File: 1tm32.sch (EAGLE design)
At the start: 38 parts, among them IC1 STM32L412RBT6P, IC2 BGM240PA32VNN3, J1 FTSH-107-01-L-DV-K-A, J2 10118192-0001LF, SW1 LL3301FF065QJ, U2 LD39050PU33R, Y1 8MHz, Y2 32.7KHz

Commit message: layout completed
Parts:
- removed J1: FTSH-107-01-L-DV-K-A, ce-capstone:FTSH-107-01-L-DV-K-A
- removed JP1: (no value), pinhead:PINHD-1X14
- removed R11: 220, ce-capstone:RT0402FRE07220RL
- removed R14: 10k, ce-capstone:RC0402FR-0710KL
- removed R5: 1K, ce-capstone:RC0402FR-071KL
- added J3: FTSH-105-01-L-D, FTSH-105-01-L-D(bt_connect):FTSH-105-01-L-D
- added J4: 20021321-00020C4LF, 20021321-00020C4LF(20head):20021321-00020C4LF
- added JP2: (no value), pinhead:PINHD-2X5
- added JP3: (no value), pinhead:PINHD-2X4
- added JP4: (no value), pinhead:PINHD-2X3
- added R10: 10K, RC0805JR-0710KL:RC0805JR-0710KL
- added R4: 220, RC0805FR-10220RL:RC0805FR-10220RL
- added R6, R7, R8, R9: 1K, RC0805FR-131KL:RC0805FR-131KL
- added U$3: LED_R, ce-capstone:SML-P12VTT86
- R1, R2, R3: device ce-capstone:RC0402FR-071KL -> RC0805FR-131KL:RC0805FR-131KL
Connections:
- removed net LED_G: JP1.10
- removed net PB13: IC1.PB13
- removed net PB14: IC1.PB14
- removed net PC0: IC1.PC0
- removed net PC1: IC1.PC1
- new net BT_RST: IC1.PA8, IC2.RESET, J3.03
- new net N$2: R1.1, U$3.A
- new net PTI_DATA: IC2.PC04, J3.10
- new net PTI_SYNC: IC2.PC05, J3.09
- net 3V3: now also J3.01, J4.1, J4.19, J4.2, JP2.4, R10.2, R6.2, R8.2, R9.2; no longer JP1.4, R14.2, R2.2, R3.2, R5.2
- net 5V: now also JP2.9, JP3.1, R2.1, R3.1; no longer J1.3, JP1.3
- net 5V_IN: now also JP2.10; no longer JP1.2
- net ADC1_IN9: now also JP3.8, R3.2
- net ADC2_IN8: now also JP3.6, R2.2
- net BOOT0: now also JP2.7, R7.1; no longer JP1.6, R1.1
- net DBG_SWCLK: now also J3.08
- net DBG_SWDIO: now also J3.07
- net DBG_SWO: now also J3.06
- net GND: now also J3.02, J4.10, J4.12, J4.14, J4.16, J4.18, J4.20, J4.4, J4.6, J4.8, JP2.6, JP2.8, JP3.3, JP3.5, JP3.7, R7.2, U$3.C; no longer J1.11, J1.5, J1.7, JP1.1, JP1.13, JP1.14, R1.2
- net I2C1_SCL: now also JP3.4, R9.1; no longer JP1.8, R3.1
- net I2C1_SDA: now also JP3.2, R8.1; no longer JP1.7, R2.1
- net LED_R: now also IC1.PB12, JP2.2, R1.2; no longer JP1.9
- net N$3: now also R4.2; no longer R11.1
- net N$5: now also R6.1; no longer R5.1
- net NRST: now also J4.15, JP2.5, R10.1; no longer IC2.RESET, J1.12, JP1.5, R14.1
- net PH1-OSC-OUT: now also R4.1; no longer R11.2
- net QUADSPI_BK1_IO0: now also JP4.4
- net QUADSPI_BK1_IO1: now also JP4.3
- net QUADSPI_BK1_IO2: now also JP4.2
- net QUADSPI_BK1_IO3: now also JP4.1
- net QUADSPI_BK1_NCS: now also JP4.6
- net QUADSPI_CLK: now also JP4.5
- net SWCLK: now also J4.9; no longer J1.6, J1.9
- net SWDIO: now also J4.7; no longer J1.4
- net SWO: now also J4.13; no longer J1.8
- net USART1_RX: now also J3.05; no longer J1.13, JP1.11
- net USART1_TX: now also J3.04; no longer J1.14, JP1.12
- net USART3_RX: now also JP2.3
- net USART3_TX: now also JP2.1
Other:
- moved on the sheet: U$1

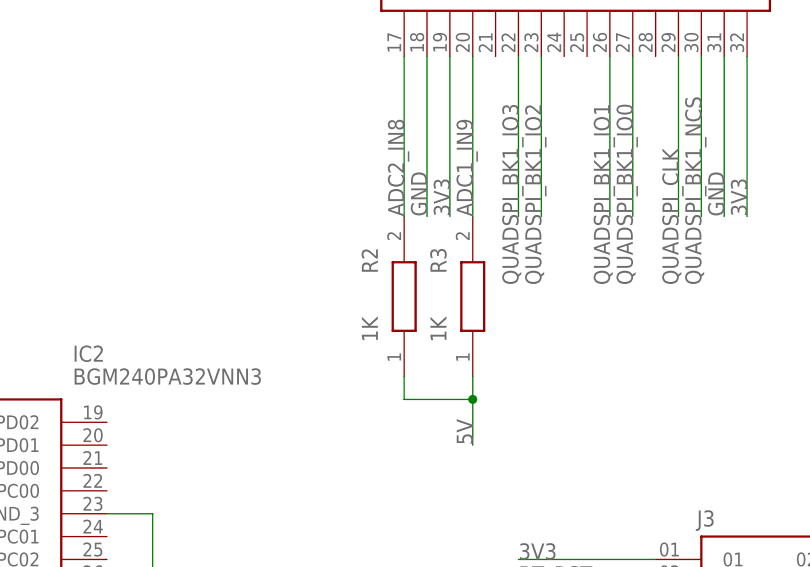
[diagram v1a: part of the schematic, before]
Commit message: add gnd vias and change adc resistors
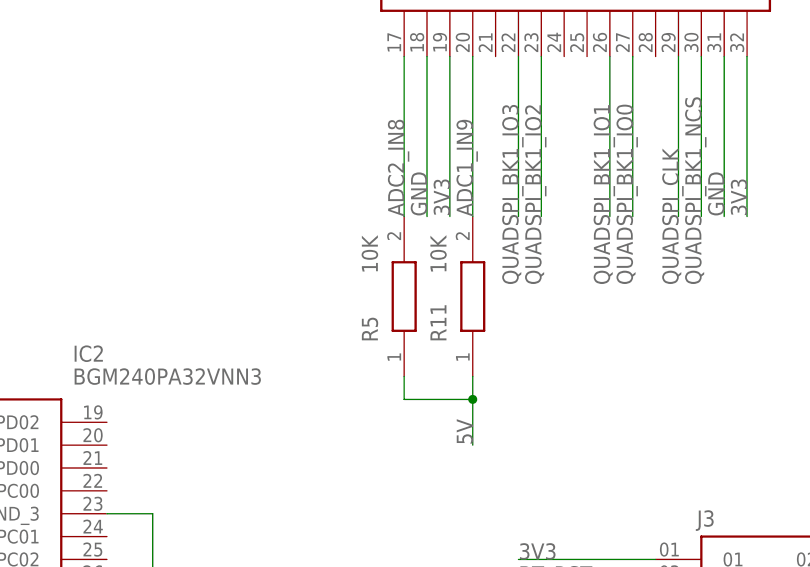
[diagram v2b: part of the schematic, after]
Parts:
- removed R2, R3: 1K, RC0805FR-131KL:RC0805FR-131KL
- added R11, R5: 10K, RC0805JR-0710KL:RC0805JR-0710KL
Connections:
- net 5V: now also R11.1, R5.1; no longer R2.1, R3.1
- net ADC1_IN9: now also R11.2; no longer R3.2
- net ADC2_IN8: now also R5.2; no longer R2.2
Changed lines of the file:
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@@
 <part name="GND10" library="supply1" library_urn="urn:adsk.eagle:library:371" deviceset="GND" device=""/>
 <part name="JP2" library="pinhead" library_urn="urn:adsk.eagle:library:325" deviceset="PINHD-2X5" device="" package3d_urn="urn:adsk.eagle:package:22470/2"/>
-<part name="R2" library="RC0805FR-131KL" deviceset="RC0805FR-131KL" device="" value="1K"/>
-<part name="R3" library="RC0805FR-131KL" deviceset="RC0805FR-131KL" device="" value="1K"/>
 <part name="JP3" library="pinhead" library_urn="urn:adsk.eagle:library:325" deviceset="PINHD-2X4" device="" package3d_urn="urn:adsk.eagle:package:22461/2"/>
 <part name="JP4" library="pinhead" library_urn="urn:adsk.eagle:library:325" deviceset="PINHD-2X3" device="" package3d_urn="urn:adsk.eagle:package:22462/2"/>
+<part name="R5" library="RC0805JR-0710KL" deviceset="RC0805JR-0710KL" device="" value="10K"/>
+<part name="R11" library="RC0805JR-0710KL" deviceset="RC0805JR-0710KL" device="" value="10K"/>
 </parts>
 <sheets>
@@
 <attribute name="VALUE" x="143.51" y="-63.5" size="1.778" layer="96"/>
 </instance>
-<instance part="R2" gate="G$1" x="22.86" y="-43.18" smashed="yes" rot="R90">
-<attribute name="NAME" x="19.05" y="-31.75" size="1.778" layer="95" rot="R90" align="center-left"/>
-<attribute name="VALUE" x="19.05" y="-39.37" size="1.778" layer="96" rot="R90" align="center-left"/>
-</instance>
-<instance part="R3" gate="G$1" x="30.48" y="-43.18" smashed="yes" rot="R90">
-<attribute name="NAME" x="26.67" y="-31.75" size="1.778" layer="95" rot="R90" align="center-left"/>
-<attribute name="VALUE" x="26.67" y="-39.37" size="1.778" layer="96" rot="R90" align="center-left"/>
-</instance>
 <instance part="JP3" gate="A" x="149.86" y="-15.24" smashed="yes">
 <attribute name="NAME" x="143.51" y="-6.985" size="1.778" layer="95"/>
@@
 <attribute name="NAME" x="143.51" y="-24.765" size="1.778" layer="95"/>
 <attribute name="VALUE" x="143.51" y="-38.1" size="1.778" layer="96"/>
+</instance>
+<instance part="R5" gate="G$1" x="22.86" y="-43.18" smashed="yes" rot="R90">
+<attribute name="NAME" x="19.05" y="-39.37" size="1.778" layer="95" rot="R90" align="center-left"/>
+<attribute name="VALUE" x="19.05" y="-31.75" size="1.778" layer="96" rot="R90" align="center-left"/>
+</instance>
+<instance part="R11" gate="G$1" x="30.48" y="-43.18" smashed="yes" rot="R90">
+<attribute name="NAME" x="26.67" y="-39.37" size="1.778" layer="95" rot="R90" align="center-left"/>
+<attribute name="VALUE" x="26.67" y="-31.75" size="1.778" layer="96" rot="R90" align="center-left"/>
 </instance>
 </instances>
@@
 </segment>
 <segment>
-<pinref part="R2" gate="G$1" pin="1"/>
 <wire x1="22.86" y1="-43.18" x2="22.86" y2="-45.72" width="0.1524" layer="91"/>
 <wire x1="22.86" y1="-45.72" x2="30.48" y2="-45.72" width="0.1524" layer="91"/>
-<pinref part="R3" gate="G$1" pin="1"/>
 <wire x1="30.48" y1="-45.72" x2="30.48" y2="-43.18" width="0.1524" layer="91"/>
 <wire x1="30.48" y1="-45.72" x2="30.48" y2="-50.8" width="0.1524" layer="91"/>
 <junction x="30.48" y="-45.72"/>
 <label x="30.48" y="-50.8" size="1.778" layer="95" rot="R90"/>
+<pinref part="R5" gate="G$1" pin="1"/>
+<pinref part="R11" gate="G$1" pin="1"/>
 </segment>
 <segment>
@@
 <wire x1="22.86" y1="-7.62" x2="22.86" y2="-25.4" width="0.1524" layer="91"/>
 <label x="22.86" y="-25.4" size="1.778" layer="95" rot="R90"/>
-<pinref part="R2" gate="G$1" pin="2"/>
+<pinref part="R5" gate="G$1" pin="2"/>
 </segment>
 <segment>
@@
 <wire x1="30.48" y1="-7.62" x2="30.48" y2="-25.4" width="0.1524" layer="91"/>
 <label x="30.48" y="-25.4" size="1.778" layer="95" rot="R90"/>
-<pinref part="R3" gate="G$1" pin="2"/>
-</segment>
-<segment>
+<pinref part="R11" gate="G$1" pin="2"/>
+</segment>
+<segment>
